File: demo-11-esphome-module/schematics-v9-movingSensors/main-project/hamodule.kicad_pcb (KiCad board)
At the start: 2 copper layers, 144.8 x 76.2 mm, 54 parts, among them J1 1017505, J2 Conn-ESP-Relays, J3 1017505, J4 Conn-Buttons, J5 Conn_01x02, J6 Conn-Esp-Sensors, J7 Conn-LedIndicators, J8 1017505, K1 G5Q-1, K2 G5Q-1, K3 G5Q-1, K4 G5Q-1, U1 ULN2003A, U2 LD1117S33TR_SOT223, U3 HCPL3700, U4 HCPL3700, U5 HCPL3700, U6 HCPL3700

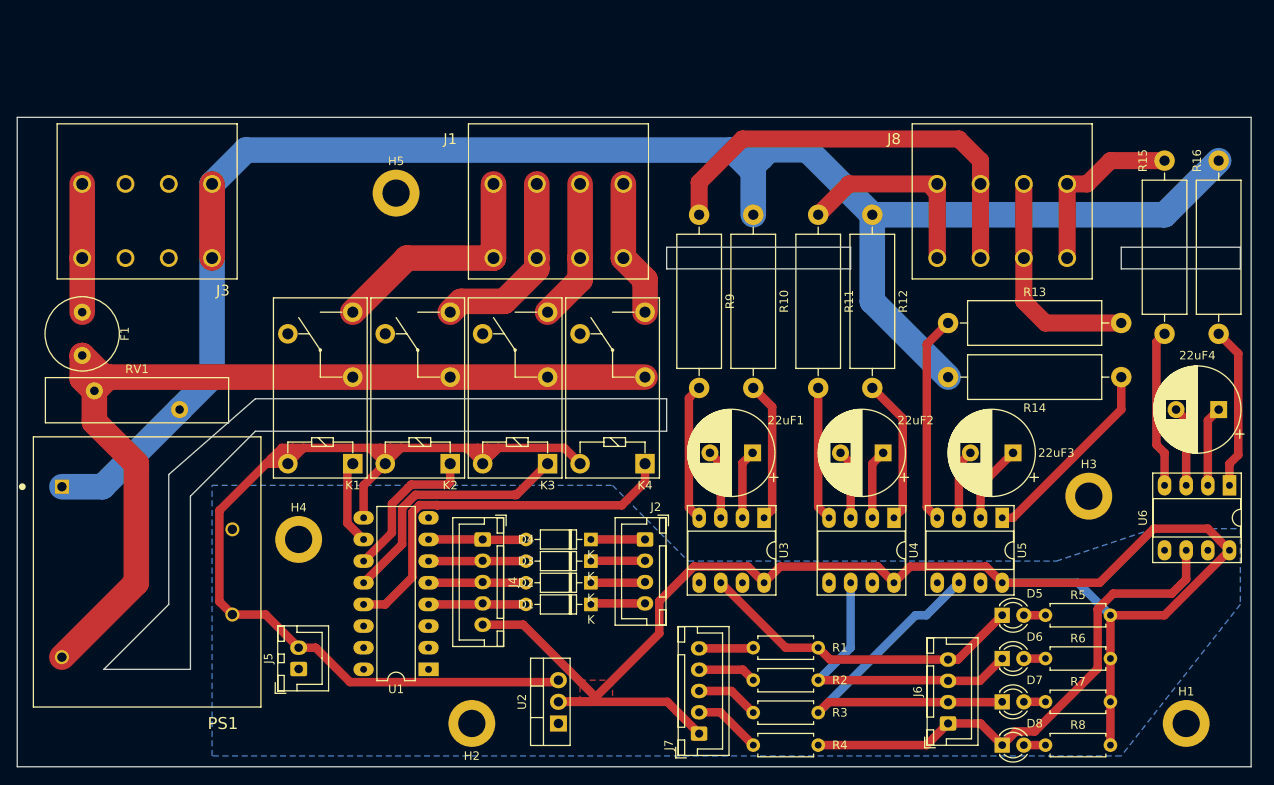
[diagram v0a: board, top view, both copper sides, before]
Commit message: arranging 22v sensing
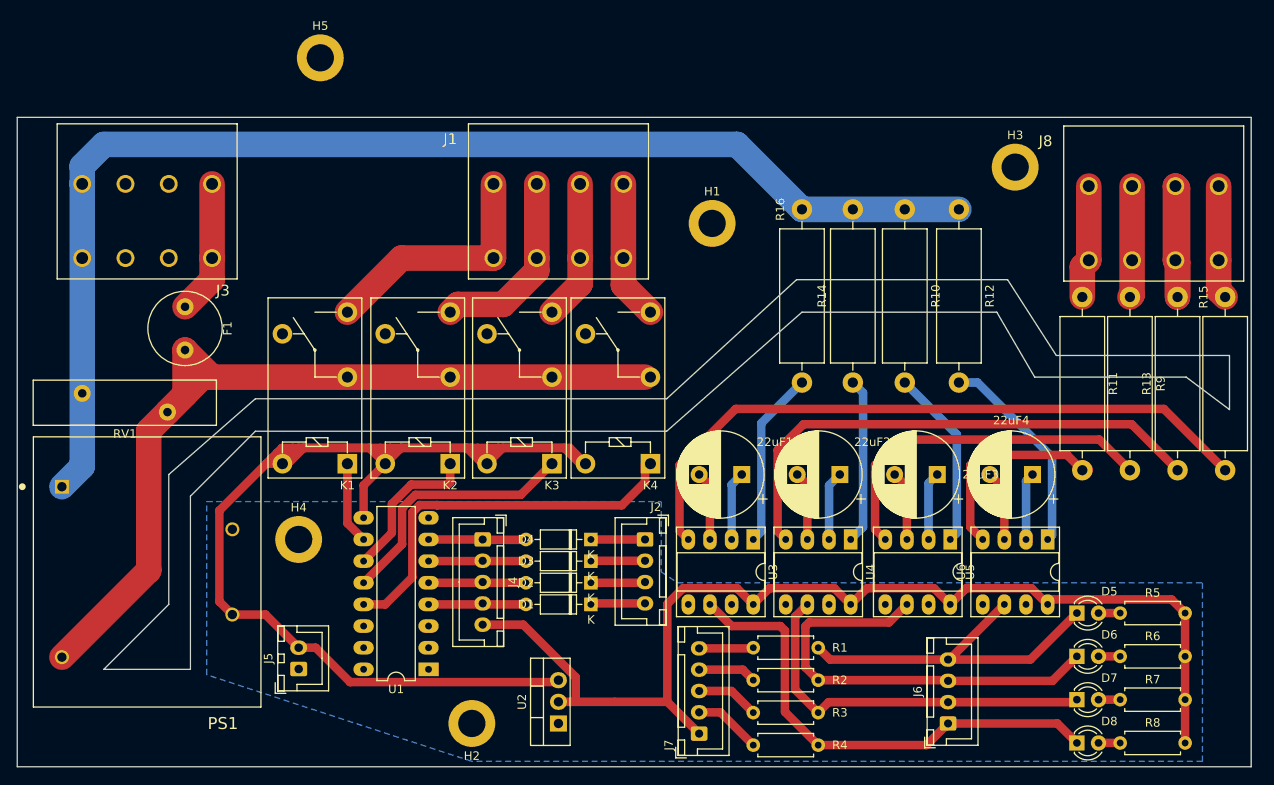
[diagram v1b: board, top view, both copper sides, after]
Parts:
- moved H1 80.9 mm to (103.1, 23.9)
- moved R9 51.5 mm to (152.1, 32.5)
- moved R16 49.2 mm to (113.7, 22.2)
- moved H3 39.6 mm to (138.7, 17.3)
- moved R11 32.5 mm to (146.6, 32.5)
- moved R13 32.0 mm to (157.7, 52.8), turned to 90 degrees
- moved R14 31.5 mm to (119.6, 42.5), turned to 90 degrees
- moved 22uF4 23.1 mm to (140.7, 53.3)
- moved U6 22.3 mm to (142.5, 61.0)
- moved H5 18.2 mm to (57.1, 4.45)
- moved R10 17.8 mm to (125.7, 22.2)
- moved J8 17.8 mm to (162.6, 28.2)
- moved R15 17.5 mm to (163.3, 32.5)
- moved F1 12.1 mm to (41.3, 33.7)
- moved RV1 11.6 mm to (29.2, 43.8), turned to 0 degrees
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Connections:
- J3 pad 1: 220VAC(N) -> Net-(F1-Pad1)
- J3 pad 2: 220VAC(N) -> Net-(F1-Pad1)
- J3 pad 7: Net-(F1-Pad1) -> 220VAC(N)
- J3 pad 8: Net-(F1-Pad1) -> 220VAC(N)
- U3 pad 1: Net-(R10-Pad2) -> Net-(R16-Pad2)
- U3 pad 4: Net-(R9-Pad2) -> Net-(R15-Pad2)
- U3 pad 6: EspSens1 -> EspSens4
- U4 pad 1: Net-(R12-Pad2) -> Net-(R14-Pad1)
- U4 pad 4: Net-(R11-Pad2) -> Net-(R13-Pad1)
- U4 pad 6: EspSens2 -> EspSens3
- U5 pad 1: Net-(R14-Pad1) -> Net-(R10-Pad2)
- U5 pad 4: Net-(R13-Pad1) -> Net-(R9-Pad2)
- U5 pad 6: EspSens3 -> EspSens2
- U6 pad 1: Net-(R16-Pad2) -> Net-(R12-Pad2)
- U6 pad 4: Net-(R15-Pad2) -> Net-(R11-Pad2)
- U6 pad 6: EspSens4 -> EspSens1
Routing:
- net 220VAC(N): track 293.8 -> 145.7 mm
- net Net-(R15-Pad2): track 18.6 -> 78.9 mm
- net 3.3V+: track 176.7 -> 129.1 mm
- net Sens1: track 51.4 -> 13.1 mm
- net Net-(R13-Pad1): track 24.4 -> 61.3 mm
- net 5V+: track 137.6 -> 172.6 mm
- net Net-(R9-Pad2): track 16.2 -> 41.9 mm
- net EspSens2: track 36.4 -> 51.5 mm
- net Sens2: track 24.8 -> 13.3 mm
- net Net-(R11-Pad2): track 15.8 -> 24.0 mm
- net Sens4: track 21.3 -> 13.3 mm
- net Net-(R12-Pad2): track 17.1 -> 24.4 mm
- net 220VAC(L): track 111.5 -> 104.2 mm
- net Net-(R10-Pad2): track 16.6 -> 21.3 mm
- net EspSens1: track 38.9 -> 42.5 mm
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- removed copper zone on F.Cu, net 3.3V+
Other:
- outline, holes or cut-outs redrawn

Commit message: varistor + F.SilkS
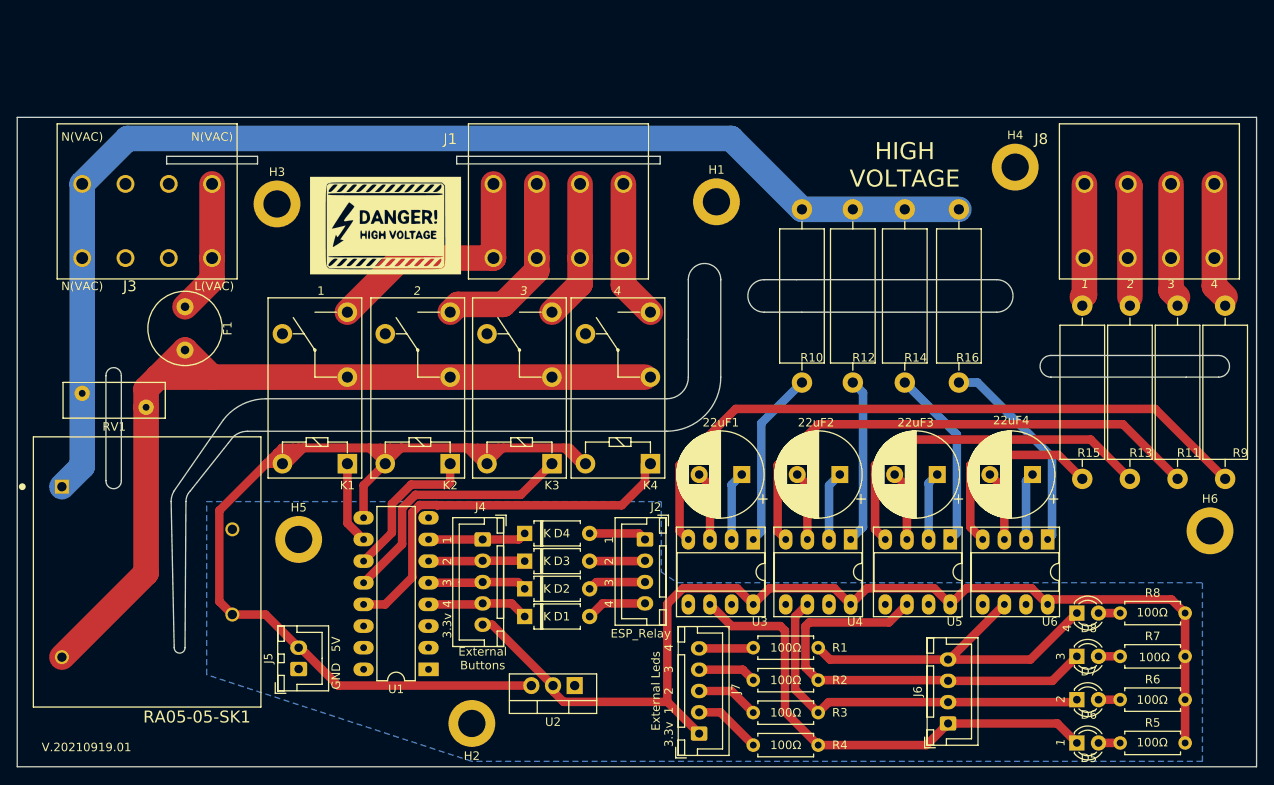
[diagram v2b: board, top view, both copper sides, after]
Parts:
- added ?: , icons:danger1_negative, F.Cu at (64.8, 24.1)
- added H3: MountingHole_Pad, MountingHole:MountingHole_3.2mm_M3_ISO14580_Pad, F.Cu at (52.1, 21.6)
- D1, D2, D3, D4: value DIODE -> D; footprint Diode_THT:D_DO-35_SOD27_P7.62mm_Horizontal -> Diode_THT:D_A-405_P7.62mm_Horizontal
- R10: renamed from R16; value 47k -> 39k2w
- R11: renamed from R13; value 47k -> 39k2w
- R12: renamed from R14; value 47k -> 39k2w
- R13: renamed from R9; value 47k -> 39k2w
- R14: renamed from R10; value 47k -> 39k2w
- R15: renamed from R11; value 47k -> 39k2w
- R16: renamed from R12; value 47k -> 39k2w
- R9: renamed from R15; value 47k -> 39k2w
- RV1: value Varistor -> Varistor250v; footprint Varistor:RV_Disc_D21.5mm_W5.3mm_P10mm -> Varistor:RV_Disc_D12mm_W4.2mm_P7.5mm
- moved H6 118.2 mm to (161.5, 59.9)
- moved D1 7.90 mm to (81.1, 70.0), turned to 0 degrees
- moved D4 7.80 mm to (81.1, 60.2), turned to 0 degrees
- moved D2 7.80 mm to (81.1, 66.8), turned to 0 degrees
- moved D3 7.77 mm to (81.1, 63.5), turned to 0 degrees
- moved U2 4.84 mm to (87.0, 78.1), turned to 180 degrees
- moved H1 2.59 mm to (103.6, 21.3)
- moved R11 1.02 mm to (157.7, 53.8)
- moved R13 1.02 mm to (152.1, 33.5)
- moved R15 1.02 mm to (146.6, 33.5)
- moved R9 1.02 mm to (163.3, 33.5)
- moved J8 0.57 mm to (162.1, 27.9)
- renumbered D8 to D5, D7 to D6, D6 to D7, D5 to D8, H3 to H4, H4 to H5, H5 to H6, R8 to R5, R7 to R6, R6 to R7, R5 to R8, PS1 to RA05-05-SK1
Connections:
- D1 pad 1: Net-(D1-Pad1) -> EspRel1
- D1 pad 2: EspRel1 -> Net-(D1-Pad2)
- D2 pad 1: Net-(D2-Pad1) -> EspRel2
- D2 pad 2: EspRel2 -> Net-(D2-Pad2)
- D3 pad 1: Net-(D3-Pad1) -> EspRel3
- D3 pad 2: EspRel3 -> Net-(D3-Pad2)
- D4 pad 1: Net-(D4-Pad1) -> EspRel4
- D4 pad 2: EspRel4 -> Net-(D4-Pad2)
- J2 pad 1: Net-(D4-Pad1) -> Net-(D4-Pad2)
- J2 pad 2: Net-(D3-Pad1) -> Net-(D3-Pad2)
- J2 pad 3: Net-(D2-Pad1) -> Net-(D2-Pad2)
- J2 pad 4: Net-(D1-Pad1) -> Net-(D1-Pad2)
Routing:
- net Sens3: track 26.2 -> 13.6 mm
- net Net-(D1-Pad2): track 0.00 -> 7.14 mm
- net Net-(D2-Pad2): track 0.00 -> 6.94 mm
- net Net-(D4-Pad2): track 0.00 -> 6.79 mm
- net Net-(D3-Pad2): track 0.00 -> 6.52 mm
- net Net-(D1-Pad1): track 6.40 -> 0.00 mm
- net Net-(D2-Pad1): track 6.38 -> 0.00 mm
- net Net-(D3-Pad1): track 6.37 -> 0.00 mm
- net Net-(D4-Pad1): track 6.35 -> 0.00 mm
- net 3.3V+: track 129.1 -> 125.7 mm
- net 5V+: track 172.6 -> 169.5 mm
- net 220VAC(N): track 145.7 -> 145.0 mm
- net Net-(R11-Pad1): track 61.3 -> 60.7 mm
- net 220VAC(L): track 104.2 -> 103.7 mm
- net EspRel1: track 11.5 -> 12.1 mm
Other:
- board size 144.8 x 76.2 mm -> 145.4 x 76.2 mm
- board text added: "1"
- board text added: "100Ω"
- board text added: "2"
- board text added: "3"
- board text added: "3.3v"
- board text added: "4"
- board text added: "5V"
- board text added: "ESP_Relay"
- board text added: "External Buttons"
- board text added: "External Leds"
- board text added: "GND"
- board text added: "HIGH VOLTAGE"
- board text added: "L(VAC)"
- board text added: "N(VAC)"
- board text added: "V.20210919.01"

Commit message: can't remember
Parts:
- moved H2 20.1 mm to (54.8, 82.9)
- moved H6 6.84 mm to (154.8, 61.1)
- moved H5 2.50 mm to (55.9, 63.1)
- renumbered RA05-05-SK1 to RA05-05-SK177
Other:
- outline, holes or cut-outs redrawn
- board text added: "39kΩ 3W"
- board text added: "ESP Sensing 220v"
- board text added: "HCPL3700"
- board text added: "L 220V"
- board text added: "LD1117AV33"
- board text added: "N 220V"
- board text added: "ULN2003A"

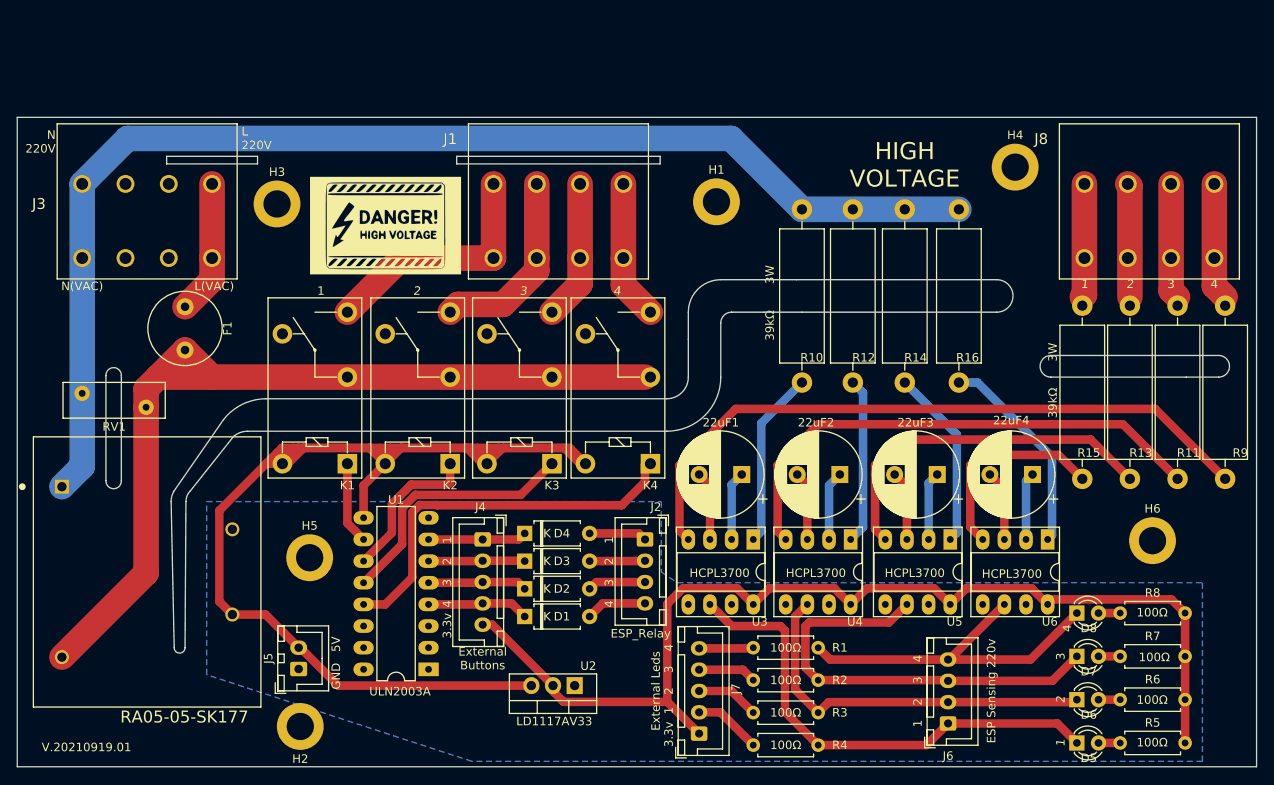
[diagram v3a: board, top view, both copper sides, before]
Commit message: adding caps
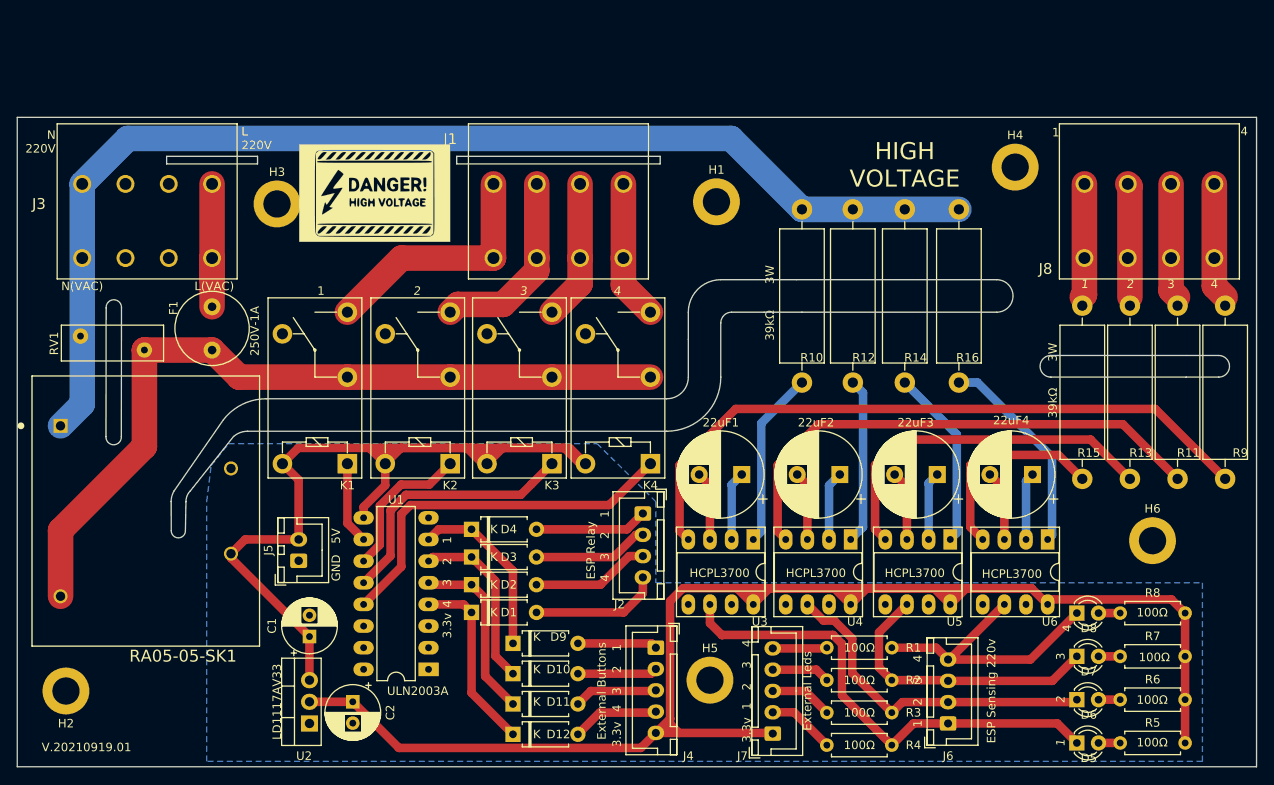
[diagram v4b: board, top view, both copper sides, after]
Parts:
- removed ?: , icons:danger1_negative
- added C1: 100uF, Capacitor_THT:CP_Radial_D6.3mm_P2.50mm, F.Cu at (55.9, 72.3)
- added C2: 100uF, Capacitor_THT:CP_Radial_D6.3mm_P2.50mm, F.Cu at (61.0, 80.0)
- added D10: D, Diode_THT:D_A-405_P7.62mm_Horizontal, F.Cu at (79.8, 76.7)
- added D11: D, Diode_THT:D_A-405_P7.62mm_Horizontal, F.Cu at (79.8, 80.3)
- added D12: D, Diode_THT:D_A-405_P7.62mm_Horizontal, F.Cu at (79.8, 83.8)
- added D9: D, Diode_THT:D_A-405_P7.62mm_Horizontal, F.Cu at (79.8, 73.2)
- added G***: LOGO, icons:danger1_negative, F.Cu at (63.5, 20.3)
- moved H5 49.1 mm to (102.9, 77.5)
- moved U2 31.4 mm to (55.9, 82.5), turned to 90 degrees
- moved H2 27.8 mm to (27.3, 78.7)
- moved J4 24.0 mm to (96.5, 73.7)
- moved J5 12.7 mm to (54.6, 63.5)
- moved J7 8.64 mm to (110.2, 83.7)
- moved R1 8.64 mm to (124.2, 73.7)
- moved R2 8.64 mm to (124.2, 77.5)
- moved R3 8.64 mm to (124.2, 81.3)
- moved R4 8.64 mm to (124.2, 85.1)
- moved RA05-05-SK1 7.15 mm to (36.7, 57.6)
- moved RV1 6.72 mm to (29.0, 37.1)
- moved D1 6.25 mm to (74.9, 69.5)
- moved D2 6.25 mm to (74.9, 66.3)
- moved D3 6.25 mm to (74.9, 63.0)
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- renumbered RA05-05-SK177 to RA05-05-SK1
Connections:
- H1 pad 1: (no net) -> Net-(H1-Pad1)
- H2 pad 1: (no net) -> Net-(H2-Pad1)
- H3 pad 1: (no net) -> Net-(H3-Pad1)
- H4 pad 1: (no net) -> Net-(H4-Pad1)
- H5 pad 1: (no net) -> Net-(H5-Pad1)
- H6 pad 1: (no net) -> Net-(H6-Pad1)
- J3 pad 3: (no net) -> Net-(J3-Pad3)
- J3 pad 4: (no net) -> Net-(J3-Pad4)
- J3 pad 5: (no net) -> Net-(J3-Pad5)
- J3 pad 6: (no net) -> Net-(J3-Pad6)
- J4 pad 1: EspRel4 -> Net-(D9-Pad2)
- J4 pad 2: EspRel3 -> Net-(D10-Pad2)
- J4 pad 3: EspRel2 -> Net-(D11-Pad2)
- J4 pad 4: EspRel1 -> Net-(D12-Pad2)
- K1 pad 4: (no net) -> Net-(K1-Pad4)
- K2 pad 4: (no net) -> Net-(K2-Pad4)
- K3 pad 4: (no net) -> Net-(K3-Pad4)
- K4 pad 4: (no net) -> Net-(K4-Pad4)
- U3 pad 7: (no net) -> Net-(U3-Pad7)
- U4 pad 7: (no net) -> Net-(U4-Pad7)
- U5 pad 7: (no net) -> Net-(U5-Pad7)
- U6 pad 7: (no net) -> Net-(U6-Pad7)
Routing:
- net 3.3V+: track 125.7 -> 208.4 mm
- net 5V+: track 169.5 -> 121.1 mm
- net EspSens2: track 51.5 -> 34.2 mm
- net Net-(D12-Pad2): track 0.00 -> 10.2 mm
- net 220VAC(L): track 103.7 -> 93.7 mm
- net Net-(D11-Pad2): track 0.00 -> 9.81 mm
- net EspRel1: track 12.1 -> 21.7 mm
- net EspRel3: track 11.3 -> 20.9 mm
- net EspRel2: track 11.6 -> 21.1 mm
- net Net-(D10-Pad2): track 0.00 -> 9.37 mm
- net Net-(D9-Pad2): track 0.00 -> 9.35 mm
- net EspRel4: track 11.6 -> 20.9 mm
- net EspSens1: track 42.5 -> 33.8 mm
- net Net-(D1-Pad2): track 7.14 -> 15.3 mm
- net 220VAC(N): track 145.0 -> 138.0 mm
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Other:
- outline, holes or cut-outs redrawn
- board text added: "250V-1A"
- board text added: "ESP Relay"
- board text removed: "ESP_Relay"

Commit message: caps are wrong way around
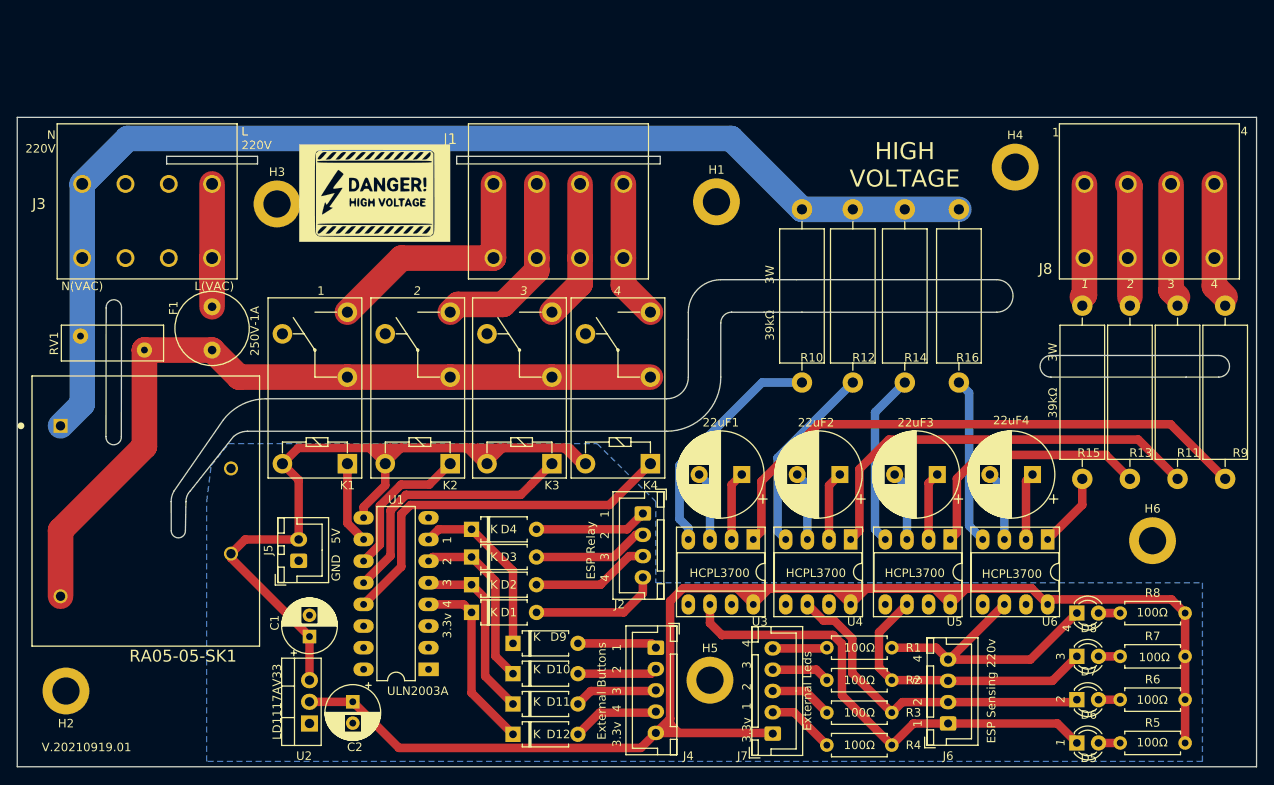
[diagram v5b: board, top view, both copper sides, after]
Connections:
- U3 pad 1: Net-(R10-Pad2) -> Net-(R9-Pad2)
- U3 pad 4: Net-(R9-Pad2) -> Net-(R10-Pad2)
- U4 pad 1: Net-(R12-Pad1) -> Net-(R11-Pad1)
- U4 pad 4: Net-(R11-Pad1) -> Net-(R12-Pad1)
- U5 pad 1: Net-(R14-Pad2) -> Net-(R13-Pad2)
- U5 pad 4: Net-(R13-Pad2) -> Net-(R14-Pad2)
- U6 pad 1: Net-(R16-Pad2) -> Net-(R15-Pad2)
- U6 pad 4: Net-(R15-Pad2) -> Net-(R16-Pad2)
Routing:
- net Net-(R15-Pad2): track 24.1 -> 8.80 mm
- net Net-(R9-Pad2): track 79.3 -> 67.1 mm
- net Net-(R13-Pad2): track 42.3 -> 30.1 mm
- net Net-(R11-Pad1): track 60.7 -> 49.4 mm
- net Net-(R10-Pad2): track 20.8 -> 27.5 mm
- net Net-(R16-Pad2): track 24.4 -> 19.6 mm
- net Net-(R12-Pad1): track 19.5 -> 22.5 mm
- net Net-(R14-Pad2): track 21.3 -> 20.4 mm
